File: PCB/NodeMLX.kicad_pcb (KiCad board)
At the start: 2 copper layers, 45 x 49 mm, 55 parts, among them J1 DS3231, J2 PIR, M1 MICROSD, U1 NodeMCUv2, U2 MLX90621

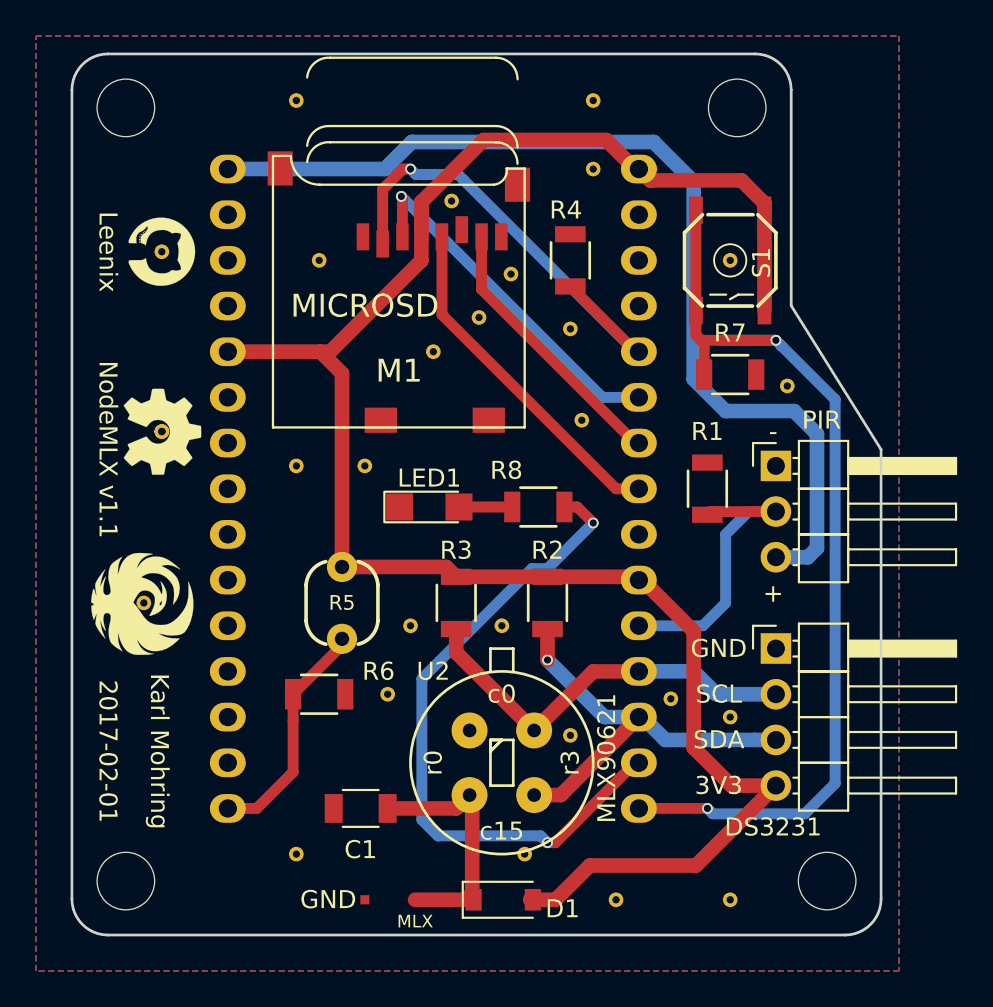
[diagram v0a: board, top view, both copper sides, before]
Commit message: Fixed PCB. Added html generators for live map
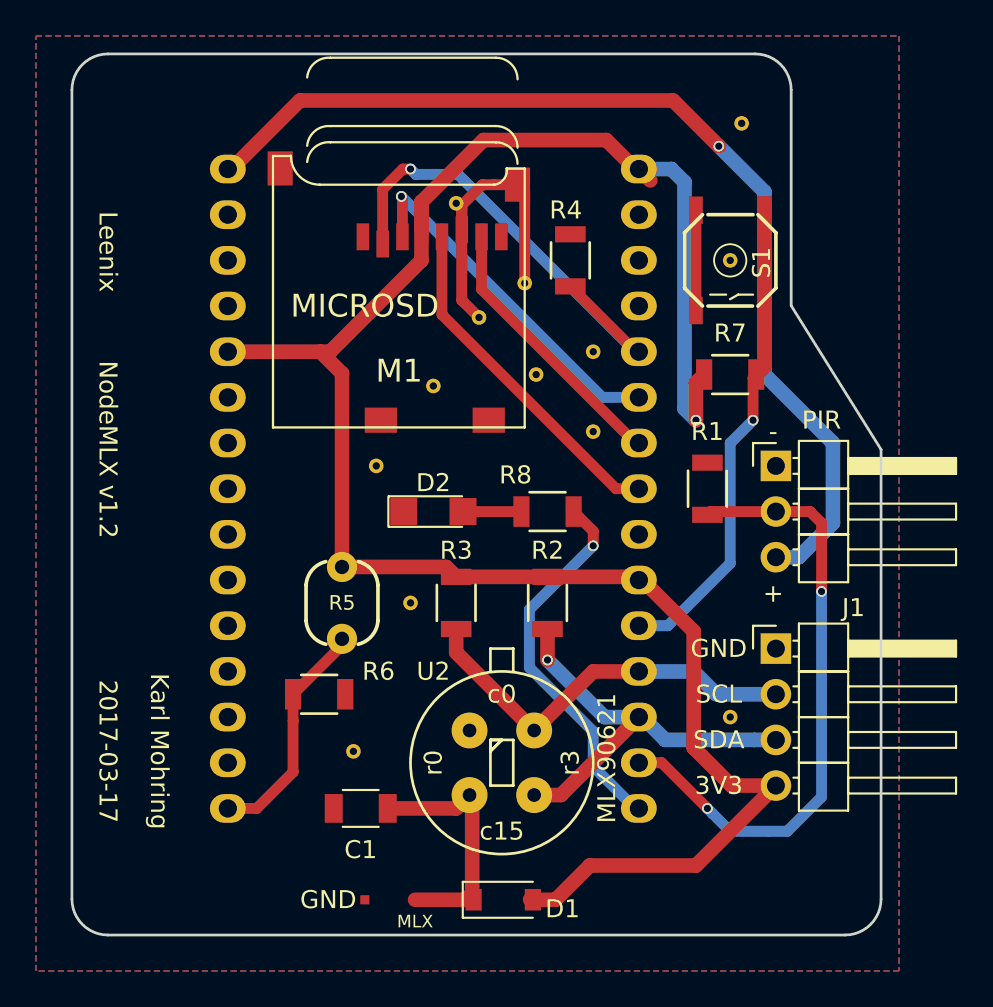
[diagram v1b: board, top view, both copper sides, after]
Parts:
- removed the ? at (45.7, 56.9)
- removed the ? at (47.0, 21.6)
- removed the ? at (30.5, 21.6)
- removed the ? at (46.4, 39.4)
- removed the ? at (42.4, 31.2)
- removed the ? at (39.1, 27.2)
- removed the ? at (54.6, 66.0)
- removed the ? at (48.3, 66.0)
- removed the ? at (43.2, 63.5)
- removed the ? at (36.8, 50.8)
- removed the ? at (30.5, 63.5)
- removed the ? at (35.6, 54.6)
- removed the ? at (47.0, 25.4)
- removed the ? at (45.7, 34.3)
- removed the ? at (34.3, 41.9)
- removed the ? at (30.5, 41.9)
- removed the ? at (38.1, 35.6)
- removed the ? at (31.8, 30.5)
- removed the ? at (57.8, 37.5)
- removed the ? at (51.3, 54.9)
- removed the ? at (22.0, 49.5)
- removed the ? at (23.0, 40.0) (x2)
- removed the ? at (23.0, 30.0)
- removed the ? at (41.9, 50.8)
- removed G***: LOGO, toolbox:phoenix-round
- removed G***: LOGO, toolbox:phoenix
- removed G***: LOGO, toolbox:octokitty_small
- removed G***: LOGO, toolbox:open-hardware-5mm
- removed LED1: RED, LEDs:LED_1206
- removed REF** (x4): MountingHole_3.2mm_M3, Mounting_Holes:MountingHole_3.2mm_M3
- added ?: , toolbox:via-0.6mm, F.Cu at (47.0, 35.6)
- added ?: , toolbox:via-0.6mm, F.Cu at (43.2, 31.8)
- added ?: , toolbox:via-0.6mm, F.Cu at (39.4, 27.3)
- added ?: , toolbox:via-0.6mm, F.Cu at (55.2, 22.9)
- added ?: , toolbox:via-0.6mm, F.Cu at (33.7, 57.8)
- added ?: , toolbox:via-0.6mm, F.Cu at (36.8, 49.5)
- added ?: , toolbox:via-0.6mm, F.Cu at (34.9, 41.9)
- added ?: , toolbox:via-0.6mm, F.Cu at (38.1, 37.5)
- added ?: , toolbox:via-0.6mm, F.Cu at (47.0, 40.0)
- added ?: , toolbox:via-0.6mm, F.Cu at (43.8, 36.8)
- added D2: RED, LEDs:LED_1206, F.Cu at (38.1, 44.5)
- J1: footprint toolbox:Pin_Header_Angled_1x04_Pitch2.54mm -> Pin_Headers:Pin_Header_Angled_1x04_Pitch2.54mm
- R8: value 130R -> 330R
- moved R8 0.57 mm to (44.5, 44.5)
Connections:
- M1 pad 1: (no net) -> Net-(M1-Pad1)
- M1 pad 8: (no net) -> Net-(M1-Pad8)
- M1 pad CD1: (no net) -> Net-(M1-PadCD1)
- M1 pad CD2: (no net) -> Net-(M1-PadCD2)
- R7 pad 1: BUTTON -> 3.3V
- R7 pad 2: GND -> BUTTON
- S1 pad 1: 3.3V -> BUTTON
- S1 pad 2: 3.3V -> BUTTON
- S1 pad 3: BUTTON -> GND
- S1 pad 4: BUTTON -> GND
- U1 pad D0: BUTTON -> LED
- U1 pad D1: LED -> PIR
- U1 pad D10: (no net) -> Net-(U1-PadD10)
- U1 pad D4: PIR -> BUTTON
- U1 pad D9: (no net) -> Net-(U1-PadD9)
- U1 pad EN: (no net) -> Net-(U1-PadEN)
- U1 pad RST: (no net) -> Net-(U1-PadRST)
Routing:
- net BUTTON: track 54.4 -> 27.3 mm, vias 2 -> 1
- net GND: track 0.00 -> 23.0 mm
- net PIR: track 16.4 -> 34.9 mm, vias 0 -> 2
- net LED: track 37.6 -> 21.1 mm, vias 2 -> 1
- net 3.3V: track 108.2 -> 114.4 mm, vias 0 -> 1
- net 5V: track 55.4 -> 57.5 mm, vias 0 -> 1
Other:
- board text added: "2017-03-17"
- board text added: "NodeMLX v1.2"
- board text removed: "2017-02-01"
- board text removed: "NodeMLX v1.1"

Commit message: Fixed PCB; added callbacks
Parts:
- added ?: , toolbox:via-0.6mm, F.Cu at (52.7, 47.0)
- added ?: , toolbox:via-0.6mm, F.Cu at (31.8, 29.2)
- added ?: , toolbox:via-0.6mm, F.Cu at (47.0, 50.2)
- added ?: , toolbox:via-0.6mm, F.Cu at (44.5, 64.1)
- added ?: , toolbox:via-0.6mm, F.Cu at (56.5, 64.8)
- added ?: , toolbox:via-0.6mm, F.Cu at (21.0, 65.4)
- added ?: , toolbox:via-0.6mm, F.Cu at (21.6, 49.5)
- added ?: , toolbox:via-0.6mm, F.Cu at (22.9, 40.6)
- added ?: , toolbox:via-0.6mm, F.Cu at (22.9, 30.5)
- added ?: , toolbox:via-0.6mm, F.Cu at (21.0, 21.6)
- added D3: 1N4148, Diodes_SMD:D_SOD-123, F.Cu at (41.9, 66.0)
- added G***: LOGO, toolbox:octokitty_small, F.Cu at (22.9, 30.5)
- added G***: LOGO, toolbox:phoenix-round, F.Cu at (21.6, 49.5)
- added G***: LOGO, toolbox:open-hardware-5mm, F.Cu at (22.9, 40.6)
- added G***: LOGO, toolbox:dickbutt_outline, B.Cu at (34.9, 59.7)
- added G***: LOGO, toolbox:phoenix, B.Cu at (38.1, 36.2)
- moved D1 5.79 mm to (36.2, 66.0)
- moved TP1 4.70 mm to (32.4, 66.0)
- moved TP2 3.81 mm to (30.5, 66.0)
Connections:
- D1 pad 2: 3.3V -> Net-(D1-Pad2)
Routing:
- net Net-(D1-Pad2): track 0.00 -> 2.41 mm
- net Net-(C1-Pad1): track 14.5 -> 13.0 mm
